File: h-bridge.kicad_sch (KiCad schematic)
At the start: 22 parts, among them Q1 BC548, Q2 IRF9540N, Q3 IRF540N, Q4 IRF9540N, Q5 IRF540N, Q6 BC548

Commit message: Small changes
Add decoupling caps, disconnect AREF from 5V, modify H-bridge resistor values
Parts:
- R10, R2: value 1K -> 10K
- R11, R3: value 100K -> 1Meg
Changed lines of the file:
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@@
       (effects (font (size 1.27 1.27)) (justify left))
     )
-    (property "Value" "1K" (id 1) (at 96.52 77.4699 0)
+    (property "Value" "10K" (id 1) (at 96.52 77.4699 0)
       (effects (font (size 1.27 1.27)) (justify left))
     )
@@
       (effects (font (size 1.27 1.27)) (justify left))
     )
-    (property "Value" "100K" (id 1) (at 96.52 116.8399 0)
+    (property "Value" "1Meg" (id 1) (at 96.52 116.8399 0)
       (effects (font (size 1.27 1.27)) (justify left))
     )
@@
   (symbol (lib_id "Device:R") (at 203.2 76.2 0) (mirror y) (unit 1)
     (in_bom yes) (on_board yes) (fields_autoplaced)
-    (property "Reference" "R10" (id 0) (at 200.66 74.9299 0)
-      (effects (font (size 1.27 1.27)) (justify left))
+    (property "Reference" "R10" (id 0) (at 205.74 74.9299 0)
+      (effects (font (size 1.27 1.27)) (justify right))
     )
-    (property "Value" "1K" (id 1) (at 200.66 77.4699 0)
-      (effects (font (size 1.27 1.27)) (justify left))
+    (property "Value" "10K" (id 1) (at 205.74 77.4699 0)
+      (effects (font (size 1.27 1.27)) (justify right))
     )
     (property "Footprint" "" (id 2) (at 204.978 76.2 90)
@@
   (symbol (lib_id "Device:R") (at 203.2 115.57 0) (mirror y) (unit 1)
     (in_bom yes) (on_board yes) (fields_autoplaced)
-    (property "Reference" "R11" (id 0) (at 200.66 114.2999 0)
-      (effects (font (size 1.27 1.27)) (justify left))
+    (property "Reference" "R11" (id 0) (at 205.74 114.2999 0)
+      (effects (font (size 1.27 1.27)) (justify right))
     )
-    (property "Value" "100K" (id 1) (at 200.66 116.8399 0)
-      (effects (font (size 1.27 1.27)) (justify left))
+    (property "Value" "1Meg" (id 1) (at 205.74 116.8399 0)
+      (effects (font (size 1.27 1.27)) (justify right))
     )
     (property "Footprint" "" (id 2) (at 204.978 115.57 90)

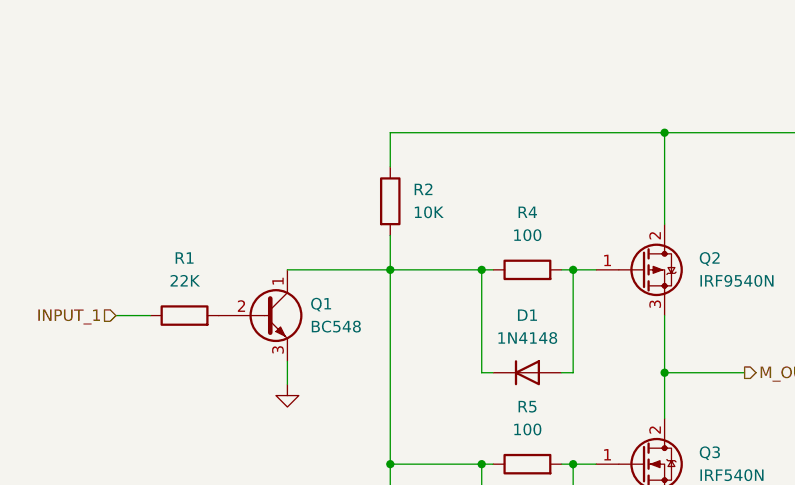
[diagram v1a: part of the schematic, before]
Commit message: Replaced steppers with pin connector
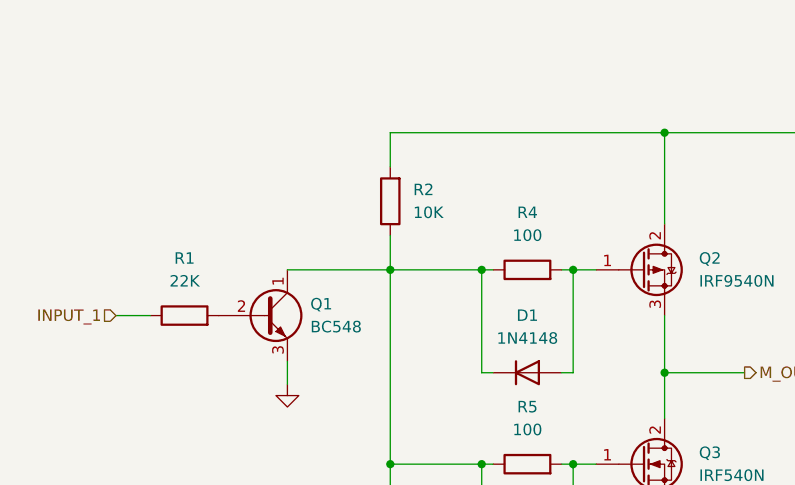
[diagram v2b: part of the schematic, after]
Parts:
- R1, R10, R11, R12, R2, R3, R4, R5, R6, R7, R8, R9: footprint (none) -> Resistor_THT:R_Axial_DIN0207_L6.3mm_D2.5mm_P10.16mm_Horizontal
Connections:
- net +12V: now also R2.2; no longer R2.1
- net at D1.1 (K), D2.1 (K), Q1.1 (C)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: now also R2.1; no longer R2.2
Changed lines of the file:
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@@
     (property "Reference" "R9" (id 0) (at 187.96 99.06 90))
     (property "Value" "100" (id 1) (at 187.96 101.6 90))
-    (property "Footprint" "" (id 2) (at 187.96 107.188 90)
+    (property "Footprint" "Resistor_THT:R_Axial_DIN0207_L6.3mm_D2.5mm_P10.16mm_Horizontal" (id 2) (at 187.96 107.188 90)
       (effects (font (size 1.27 1.27)) hide)
     )
@@
     (property "Reference" "R12" (id 0) (at 226.06 82.55 90))
     (property "Value" "22K" (id 1) (at 226.06 85.09 90))
-    (property "Footprint" "" (id 2) (at 226.06 90.678 90)
+    (property "Footprint" "Resistor_THT:R_Axial_DIN0207_L6.3mm_D2.5mm_P10.16mm_Horizontal" (id 2) (at 226.06 90.678 90)
       (effects (font (size 1.27 1.27)) hide)
     )
@@
     (property "Reference" "R4" (id 0) (at 109.22 77.47 90))
     (property "Value" "100" (id 1) (at 109.22 80.01 90))
-    (property "Footprint" "" (id 2) (at 109.22 85.598 90)
+    (property "Footprint" "Resistor_THT:R_Axial_DIN0207_L6.3mm_D2.5mm_P10.16mm_Horizontal" (id 2) (at 109.22 85.598 90)
       (effects (font (size 1.27 1.27)) hide)
     )
     (property "Datasheet" "~" (id 3) (at 109.22 83.82 0)
-      (effects (font (size 1.27 1.27)) hide)
-    )
-    (pin "1")
-    (pin "2")
-  )
-  (symbol (lib_id "Device:R") (at 93.98 76.2 0) (unit 1)
-    (in_bom yes) (on_board yes) (fields_autoplaced)
-    (property "Reference" "R2" (id 0) (at 96.52 74.9299 0)
-      (effects (font (size 1.27 1.27)) (justify left))
-    )
-    (property "Value" "10K" (id 1) (at 96.52 77.4699 0)
-      (effects (font (size 1.27 1.27)) (justify left))
-    )
-    (property "Footprint" "" (id 2) (at 92.202 76.2 90)
-      (effects (font (size 1.27 1.27)) hide)
-    )
-    (property "Datasheet" "~" (id 3) (at 93.98 76.2 0)
       (effects (font (size 1.27 1.27)) hide)
     )
@@
       (effects (font (size 1.27 1.27)) (justify left))
     )
-    (property "Footprint" "" (id 2) (at 92.202 115.57 90)
+    (property "Footprint" "Resistor_THT:R_Axial_DIN0207_L6.3mm_D2.5mm_P10.16mm_Horizontal" (id 2) (at 92.202 115.57 90)
       (effects (font (size 1.27 1.27)) hide)
     )
@@
     (property "Reference" "R1" (id 0) (at 71.12 82.55 90))
     (property "Value" "22K" (id 1) (at 71.12 85.09 90))
-    (property "Footprint" "" (id 2) (at 71.12 90.678 90)
+    (property "Footprint" "Resistor_THT:R_Axial_DIN0207_L6.3mm_D2.5mm_P10.16mm_Horizontal" (id 2) (at 71.12 90.678 90)
       (effects (font (size 1.27 1.27)) hide)
     )
@@
       (effects (font (size 1.27 1.27)) (justify left))
     )
-    (property "Footprint" "" (id 2) (at 122.682 115.57 90)
+    (property "Footprint" "Resistor_THT:R_Axial_DIN0207_L6.3mm_D2.5mm_P10.16mm_Horizontal" (id 2) (at 122.682 115.57 90)
       (effects (font (size 1.27 1.27)) hide)
     )
@@
       (effects (font (size 1.27 1.27)) (justify right))
     )
-    (property "Footprint" "" (id 2) (at 204.978 76.2 90)
+    (property "Footprint" "Resistor_THT:R_Axial_DIN0207_L6.3mm_D2.5mm_P10.16mm_Horizontal" (id 2) (at 204.978 76.2 90)
       (effects (font (size 1.27 1.27)) hide)
     )
@@
       (effects (font (size 1.27 1.27)) (justify left))
     )
-    (property "Footprint" "" (id 2) (at 174.498 115.57 90)
+    (property "Footprint" "Resistor_THT:R_Axial_DIN0207_L6.3mm_D2.5mm_P10.16mm_Horizontal" (id 2) (at 174.498 115.57 90)
       (effects (font (size 1.27 1.27)) hide)
     )
@@
       (effects (font (size 1.27 1.27)) (justify right))
     )
-    (property "Footprint" "" (id 2) (at 204.978 115.57 90)
+    (property "Footprint" "Resistor_THT:R_Axial_DIN0207_L6.3mm_D2.5mm_P10.16mm_Horizontal" (id 2) (at 204.978 115.57 90)
       (effects (font (size 1.27 1.27)) hide)
     )
@@
     (property "Reference" "R5" (id 0) (at 109.22 99.06 90))
     (property "Value" "100" (id 1) (at 109.22 101.6 90))
-    (property "Footprint" "" (id 2) (at 109.22 107.188 90)
+    (property "Footprint" "Resistor_THT:R_Axial_DIN0207_L6.3mm_D2.5mm_P10.16mm_Horizontal" (id 2) (at 109.22 107.188 90)
       (effects (font (size 1.27 1.27)) hide)
     )
@@
     (property "Reference" "R8" (id 0) (at 187.96 77.47 90))
     (property "Value" "100" (id 1) (at 187.96 80.01 90))
-    (property "Footprint" "" (id 2) (at 187.96 85.598 90)
+    (property "Footprint" "Resistor_THT:R_Axial_DIN0207_L6.3mm_D2.5mm_P10.16mm_Horizontal" (id 2) (at 187.96 85.598 90)
       (effects (font (size 1.27 1.27)) hide)
     )
@@
     (pin "3")
   )
+  (symbol (lib_id "Device:R") (at 93.98 76.2 180) (unit 1)
+    (in_bom yes) (on_board yes) (fields_autoplaced)
+    (property "Reference" "R2" (id 0) (at 96.52 74.9299 0)
+      (effects (font (size 1.27 1.27)) (justify right))
+    )
+    (property "Value" "10K" (id 1) (at 96.52 77.4699 0)
+      (effects (font (size 1.27 1.27)) (justify right))
+    )
+    (property "Footprint" "Resistor_THT:R_Axial_DIN0207_L6.3mm_D2.5mm_P10.16mm_Horizontal" (id 2) (at 95.758 76.2 90)
+      (effects (font (size 1.27 1.27)) hide)
+    )
+    (property "Datasheet" "~" (id 3) (at 93.98 76.2 0)
+      (effects (font (size 1.27 1.27)) hide)
+    )
+    (pin "1")
+    (pin "2")
+  )
   (sheet_instances
